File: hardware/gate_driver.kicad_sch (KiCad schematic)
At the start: 15 parts, among them U4 DRV8353SRTAR

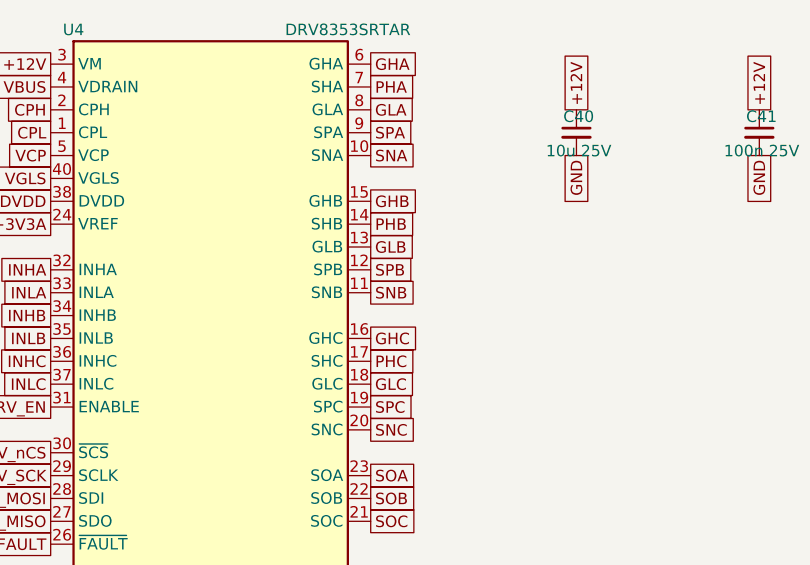
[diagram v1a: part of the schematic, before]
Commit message: Layout rev B: top-side two-shunt power stage, 5.0SMDJ60A TVS, crystal by the MCU
Commutation loop 5.0 -> 3.0 nH (FastHenry), 60 V hot-plug peak 106 -> 96 V.
Re-placed and re-routed (Freerouting + tools/hand_route.py); DRC: 0 unconnected,
only the MD80-inherent AUX1/screw courtyard overlap. Docs and sims updated.

Co-Authored-By: Claude Opus 5.5 (1M context) <noreply@anthropic.com>
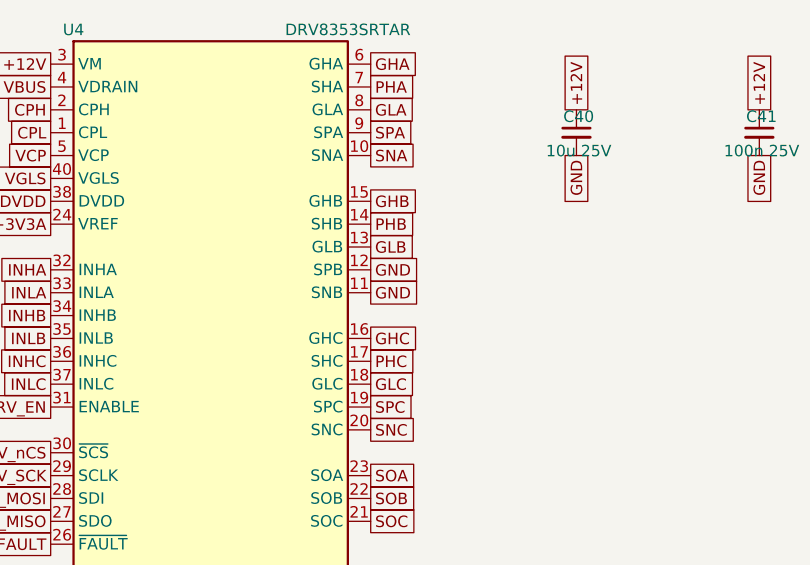
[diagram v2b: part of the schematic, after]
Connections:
- net SNB is gone; now on net GND: U4.11 (SNB)
- net SPB is gone; now on net GND: U4.12 (SPB)
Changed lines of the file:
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@@
 		)
 	)
-	(global_label "SNB"
+	(global_label "GND"
 		(shape passive)
 		(at 76.2 59.69 0)
@@
 		)
 	)
-	(global_label "SPB"
+	(global_label "GND"
 		(shape passive)
 		(at 76.2 57.15 0)
